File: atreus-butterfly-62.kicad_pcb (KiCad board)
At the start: 2 copper layers, 135.2 x 118.8 mm, 85 parts, among them J1 USB_OTG, J2 Conn_01x04, SW1 SW_Push, SW10 SW_Push, SW11 SW_Push, SW12 SW_Push, SW13 SW_Push, SW14 SW_Push, SW15 SW_Push, SW16 SW_Push, SW17 SW_Push, SW18 SW_Push, SW19 SW_Push, SW2 SW_Push, SW20 SW_Push, SW21 SW_Push, SW22 SW_Push, SW23 SW_Push, SW24 SW_Push, SW25 SW_Push, SW26 SW_Push, SW27 SW_Push, SW28 SW_Push, SW29 SW_Push, SW3 SW_Push, SW30 SW_Push, SW31 SW_Push, SW32 SW_Push, SW4 SW_Push, SW5 SW_Push, SW6 SW_Push, SW7 SW_Push, SW8 SW_Push, SW9 SW_Push, U1 ATMEGA32U4-MU, Y1 Crystal

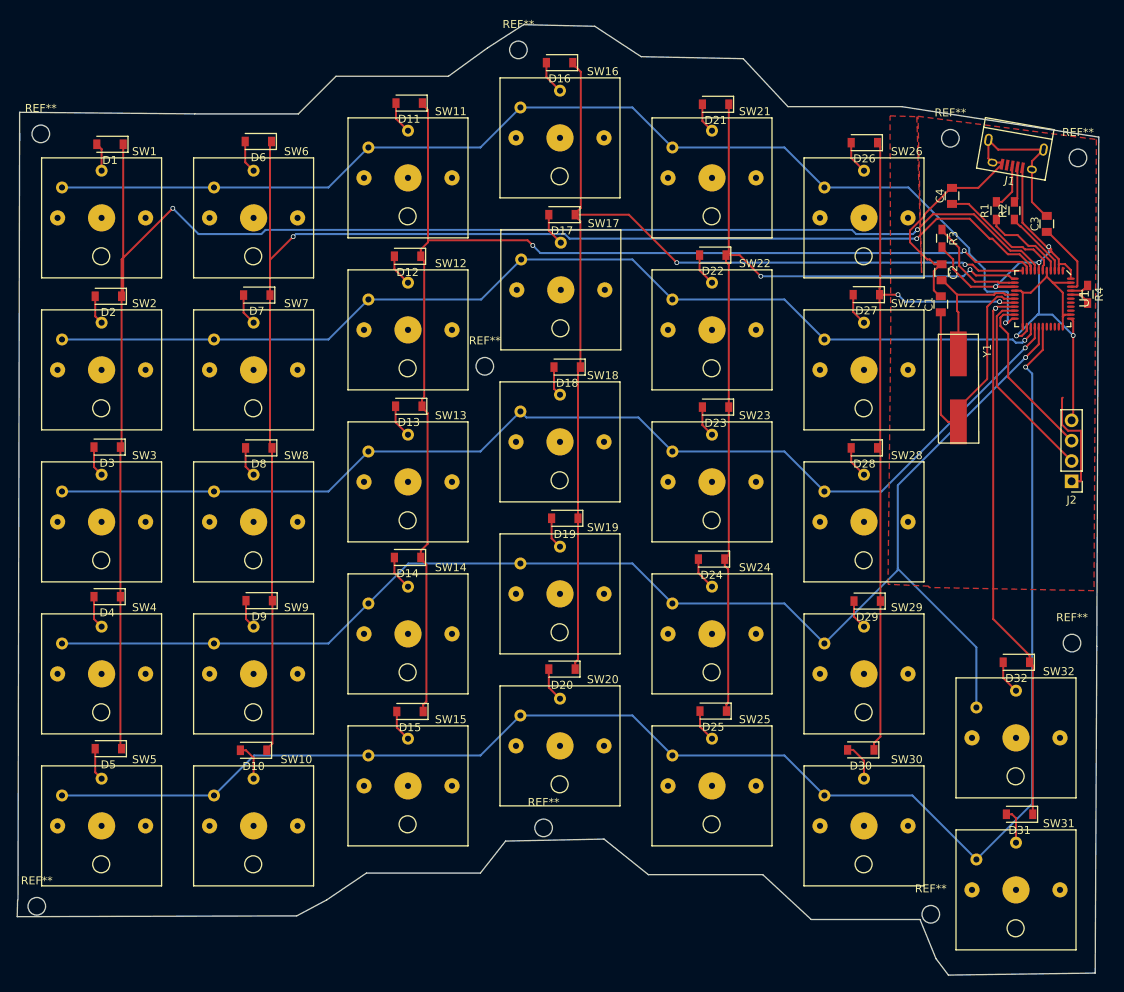
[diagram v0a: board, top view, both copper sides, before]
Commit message: add correct switch footprint and fix routing
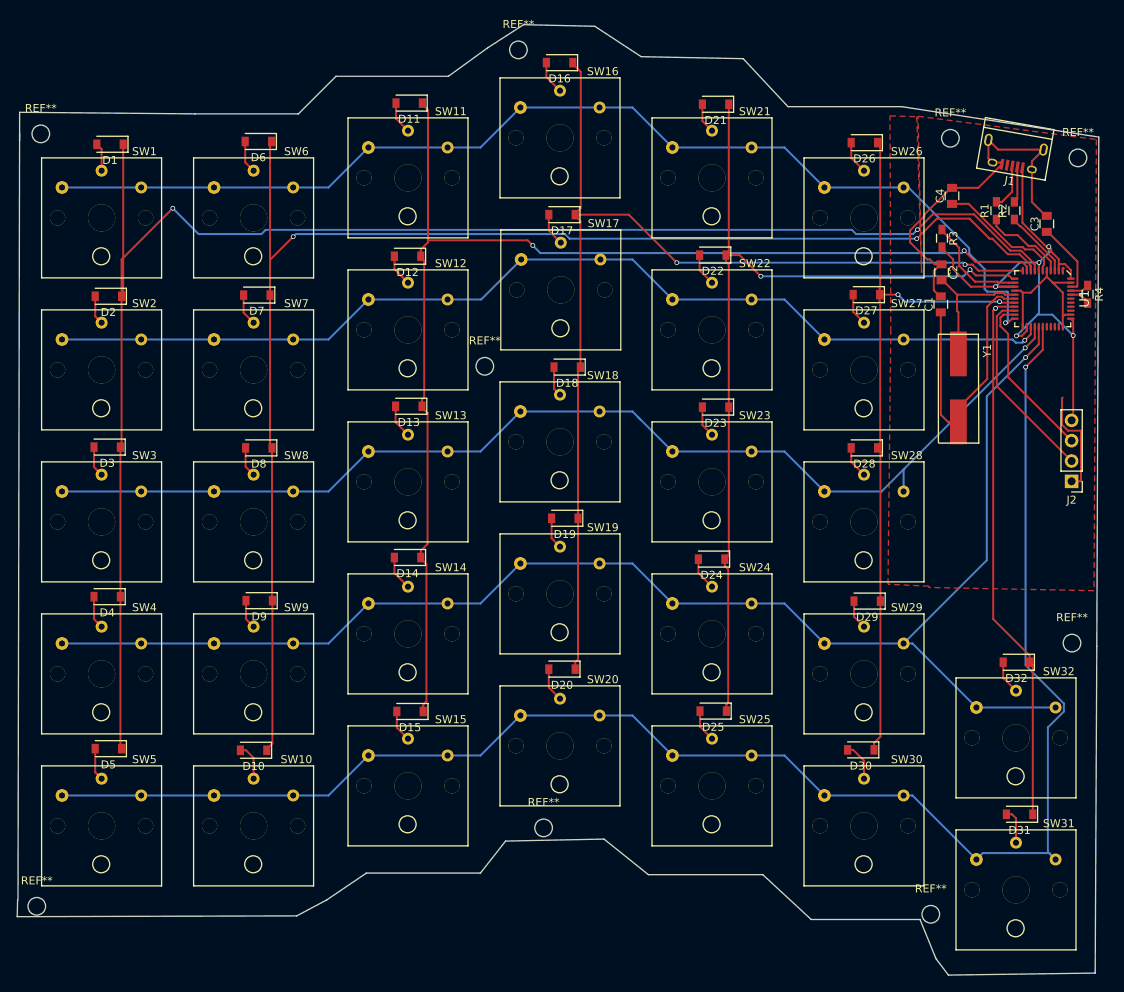
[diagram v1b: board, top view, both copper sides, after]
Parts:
- SW1, SW10, SW11, SW12, SW13, SW14, SW15, SW16, SW17, SW18, SW19, SW2, SW20, SW21, SW22, SW23, SW24, SW25, SW26, SW27, SW28, SW29, SW3, SW30, SW31, SW32, SW4, SW5, SW6, SW7, SW8, SW9: footprint ourglass_v7:Kailh_low_profile -> kailh:Kailh_low_profile
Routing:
- net /Row_5: track 196.6 -> 207.2 mm
- net /Row_4: track 175.7 -> 182.4 mm
- net /Row_3: track 139.3 -> 142.6 mm

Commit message: more stuff done no idea really
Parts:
- U1: footprint ourglass_v7:QFN_44 -> Package_DFN_QFN:QFN-44-1EP_7x7mm_P0.5mm_EP5.15x5.15mm
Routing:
- net GND: track 81.9 -> 54.8 mm
- net VCC: track 73.8 -> 71.3 mm
